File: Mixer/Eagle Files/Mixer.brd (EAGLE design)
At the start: 94 x 59 mm, 50 parts, among them CON1 1-770875-01-770875-0_VERTICAL, IC1 LM741P, IC2 LM741P, T1 2N3904

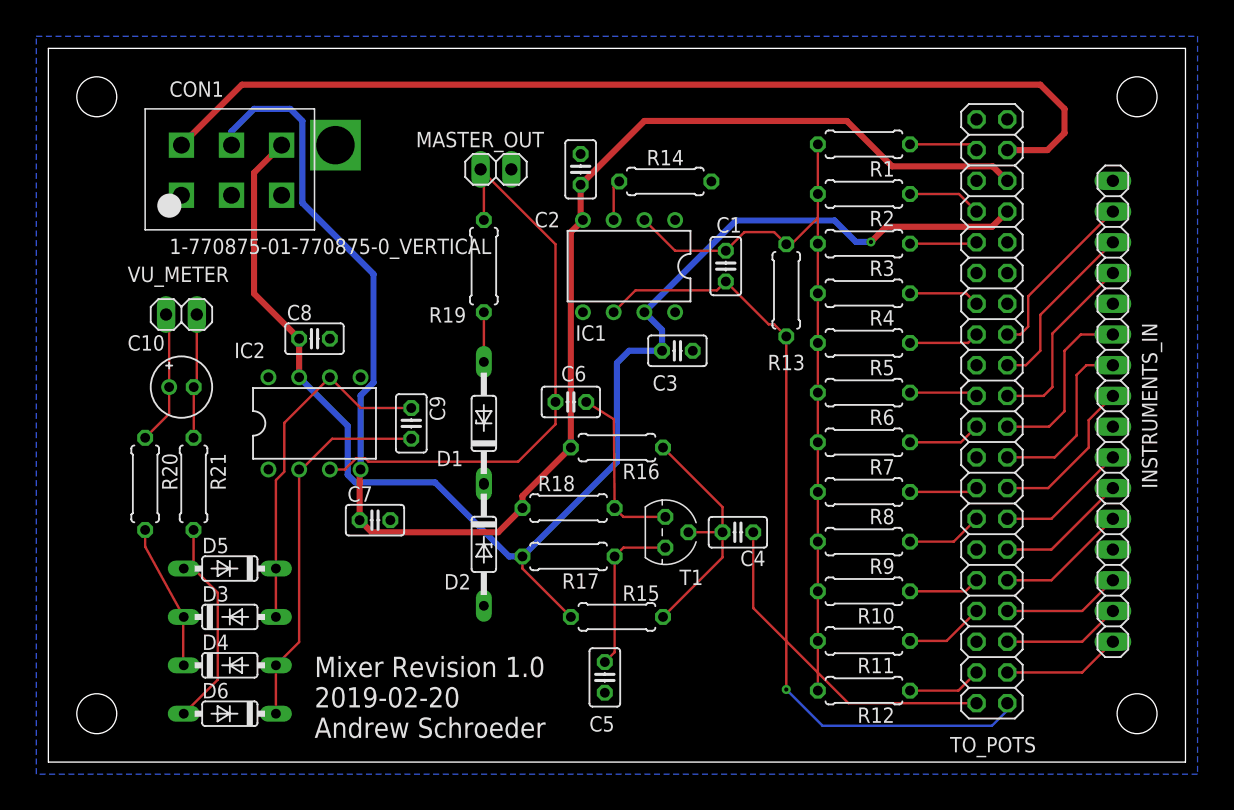
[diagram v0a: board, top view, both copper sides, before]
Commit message: Ran DRC and fixed errors. Generated CAM files and updated images.
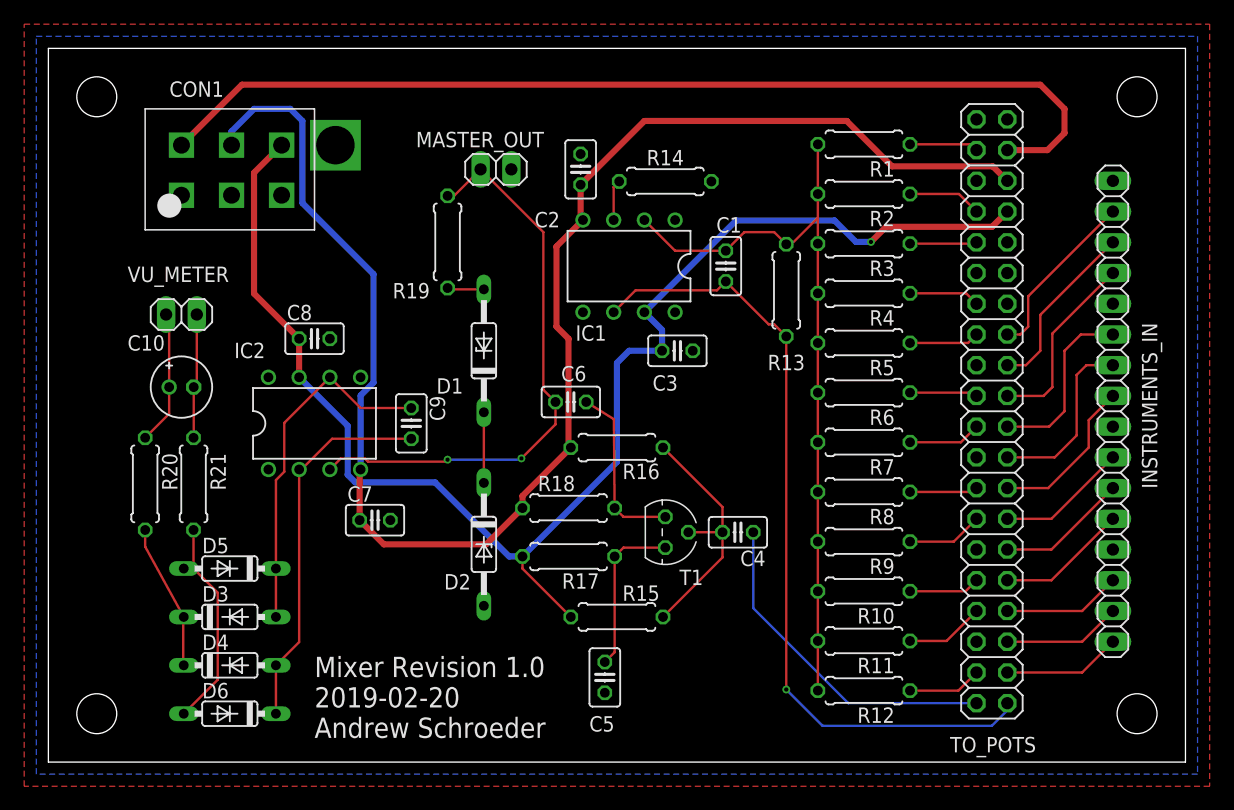
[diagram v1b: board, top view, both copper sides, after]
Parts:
- U$5: device frames:A4L-LOC -> frames:A5L-LOC
- moved U$5 39.8 mm to (-48.0, -39.0)
- moved D1 6.00 mm to (36.0, 34.0)
- moved R19 3.61 mm to (33.0, 43.0)
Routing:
- net N$16: track 0.16 -> 5.84 mm
- net -12V: track 127.2 -> 129.0 mm
- net INST7_IN: track 14.3 -> 13.2 mm
- net N$12: track 4.11 -> 3.05 mm
- net INST12_IN: track 15.4 -> 14.4 mm
- net SIG_OUT: track 48.4 -> 47.7 mm, vias 0 -> 2
- added copper zone on layer 1, net GND
